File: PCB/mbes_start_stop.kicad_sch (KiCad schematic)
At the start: 17 parts

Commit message: fixes
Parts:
- RA41: renamed from RA?; value 10K -> 100K
- gave numbers to parts that had none: 16
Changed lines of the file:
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@@
   (symbol (lib_id "Connector_Generic:Conn_01x03") (at 159.2072 78.2828 0) (mirror x) (unit 1)
     (in_bom yes) (on_board yes) (fields_autoplaced)
-    (property "Reference" "koso-?" (id 0) (at 159.2072 71.882 0))
+    (property "Reference" "koso-1" (id 0) (at 159.2072 71.882 0))
     (property "Value" "Conn_01x03" (id 1) (at 162.4076 77.0129 0)
       (effects (font (size 1.27 1.27)) (justify left) hide)
@@
   (symbol (lib_id "Device:R") (at 138.2776 97.4852 90) (unit 1)
     (in_bom yes) (on_board yes)
-    (property "Reference" "RA?" (id 0) (at 138.2776 103.8352 90)
+    (property "Reference" "RA43" (id 0) (at 138.2776 103.8352 90)
       (effects (font (size 1.27 1.27)) hide)
     )
@@
   (symbol (lib_id "Transistor_BJT:BC337") (at 81.1784 145.5928 270) (unit 1)
     (in_bom yes) (on_board yes)
-    (property "Reference" "Q?" (id 0) (at 82.4485 150.9268 0)
+    (property "Reference" "Q11" (id 0) (at 82.4485 150.9268 0)
       (effects (font (size 1.27 1.27)) (justify left) hide)
     )
@@
   (symbol (lib_id "Device:R") (at 146.1008 130.4544 90) (unit 1)
     (in_bom yes) (on_board yes)
-    (property "Reference" "RA?" (id 0) (at 146.1008 136.8044 90)
+    (property "Reference" "RA44" (id 0) (at 146.1008 136.8044 90)
       (effects (font (size 1.27 1.27)) hide)
     )
@@
   (symbol (lib_id "power:GND") (at 122.5296 154.9908 0) (unit 1)
     (in_bom yes) (on_board yes) (fields_autoplaced)
-    (property "Reference" "#PWR?" (id 0) (at 122.5296 161.3408 0)
+    (property "Reference" "#PWR0108" (id 0) (at 122.5296 161.3408 0)
       (effects (font (size 1.27 1.27)) hide)
     )
@@
   (symbol (lib_id "Device:R") (at 95.9104 59.8932 180) (unit 1)
     (in_bom yes) (on_board yes)
-    (property "Reference" "RA?" (id 0) (at 102.2604 59.8932 90)
+    (property "Reference" "RA30" (id 0) (at 102.2604 59.8932 90)
       (effects (font (size 1.27 1.27)) hide)
     )
@@
   (symbol (lib_id "Device:R") (at 90.932 116.8908 180) (unit 1)
     (in_bom yes) (on_board yes)
-    (property "Reference" "RA?" (id 0) (at 97.282 116.8908 90)
+    (property "Reference" "RA29" (id 0) (at 97.282 116.8908 90)
       (effects (font (size 1.27 1.27)) hide)
     )
@@
   (symbol (lib_id "Transistor_BJT:BC327") (at 110.5408 76.4032 0) (mirror x) (unit 1)
     (in_bom yes) (on_board yes)
-    (property "Reference" "Q?" (id 0) (at 107.7468 74.1172 90)
+    (property "Reference" "Q18" (id 0) (at 107.7468 74.1172 90)
       (effects (font (size 1.27 1.27)) hide)
     )
@@
   (symbol (lib_id "Device:R") (at 90.932 107.1372 180) (unit 1)
     (in_bom yes) (on_board yes)
-    (property "Reference" "RA?" (id 0) (at 97.282 107.1372 90)
+    (property "Reference" "RA23" (id 0) (at 97.282 107.1372 90)
       (effects (font (size 1.27 1.27)) hide)
     )
@@
   (symbol (lib_id "power:GND") (at 153.2128 82.8548 0) (unit 1)
     (in_bom yes) (on_board yes) (fields_autoplaced)
-    (property "Reference" "#PWR?" (id 0) (at 153.2128 89.2048 0)
+    (property "Reference" "#PWR0106" (id 0) (at 153.2128 89.2048 0)
       (effects (font (size 1.27 1.27)) hide)
     )
@@
   (symbol (lib_id "Relay:RT42xxxx") (at 104.902 137.9728 90) (unit 1)
     (in_bom yes) (on_board yes)
-    (property "Reference" "K?" (id 0) (at 104.902 117.9068 90)
+    (property "Reference" "K1" (id 0) (at 104.902 117.9068 90)
       (effects (font (size 1.27 1.27)) hide)
     )
@@
   (symbol (lib_id "Device:R") (at 90.8304 83.82 180) (unit 1)
     (in_bom yes) (on_board yes)
-    (property "Reference" "RA?" (id 0) (at 97.1804 83.82 90)
+    (property "Reference" "RA8" (id 0) (at 97.1804 83.82 90)
       (effects (font (size 1.27 1.27)) hide)
     )
@@
   (symbol (lib_id "Device:R") (at 101.6508 76.4032 270) (unit 1)
     (in_bom yes) (on_board yes)
-    (property "Reference" "RA?" (id 0) (at 101.6508 70.0532 90)
+    (property "Reference" "RA33" (id 0) (at 101.6508 70.0532 90)
       (effects (font (size 1.27 1.27)) hide)
     )
@@
   (symbol (lib_id "Transistor_BJT:BC327") (at 98.9076 110.8964 0) (unit 1)
     (in_bom yes) (on_board yes)
-    (property "Reference" "Q?" (id 0) (at 96.1136 113.1824 90)
+    (property "Reference" "Q16" (id 0) (at 96.1136 113.1824 90)
       (effects (font (size 1.27 1.27)) hide)
     )
@@
   (symbol (lib_id "power:+12V") (at 120.142 54.4068 0) (unit 1)
     (in_bom yes) (on_board yes) (fields_autoplaced)
-    (property "Reference" "#PWR?" (id 0) (at 120.142 58.2168 0)
+    (property "Reference" "#PWR0102" (id 0) (at 120.142 58.2168 0)
       (effects (font (size 1.27 1.27)) hide)
     )
@@
   (symbol (lib_id "Device:R") (at 126.1872 113.538 0) (unit 1)
     (in_bom yes) (on_board yes)
-    (property "Reference" "RA?" (id 0) (at 119.8372 113.538 90)
-      (effects (font (size 1.27 1.27)) hide)
-    )
-    (property "Value" "10K" (id 1) (at 126.1872 113.538 90))
+    (property "Reference" "RA41" (id 0) (at 119.8372 113.538 90)
+      (effects (font (size 1.27 1.27)) hide)
+    )
+    (property "Value" "100K" (id 1) (at 126.1872 113.538 90))
     (property "Footprint" "Resistor_THT:R_Axial_DIN0207_L6.3mm_D2.5mm_P7.62mm_Horizontal" (id 2) (at 124.4092 113.538 90)
       (effects (font (size 1.27 1.27)) hide)
@@
   (symbol (lib_id "Device:R") (at 101.6508 65.1256 270) (unit 1)
     (in_bom yes) (on_board yes)
-    (property "Reference" "RA?" (id 0) (at 101.6508 58.7756 90)
+    (property "Reference" "RA31" (id 0) (at 101.6508 58.7756 90)
       (effects (font (size 1.27 1.27)) hide)
     )
@@
   (symbol (lib_id "Transistor_BJT:BC337") (at 90.8304 72.7456 270) (mirror x) (unit 1)
     (in_bom yes) (on_board yes)
-    (property "Reference" "Q?" (id 0) (at 92.1005 67.4116 0)
+    (property "Reference" "Q13" (id 0) (at 92.1005 67.4116 0)
       (effects (font (size 1.27 1.27)) (justify left) hide)
     )
@@
   (symbol (lib_id "Transistor_BJT:BC327") (at 110.5408 65.1256 0) (unit 1)
     (in_bom yes) (on_board yes)
-    (property "Reference" "Q?" (id 0) (at 107.7468 67.4116 90)
+    (property "Reference" "Q17" (id 0) (at 107.7468 67.4116 90)
       (effects (font (size 1.27 1.27)) hide)
     )
@@
   (symbol (lib_id "Transistor_BJT:BC337") (at 88.392 128.8288 0) (unit 1)
     (in_bom yes) (on_board yes)
-    (property "Reference" "Q?" (id 0) (at 84.963 125.6538 0)
-      (effects (font (size 1.27 1.27)) (justify left) hide)
-    )
+    (property "Reference" "Q12" (id 0) (at 84.963 125.6538 0)
+      (effects (font (size 1.27 1.27)) (justify left) hide)
+    )

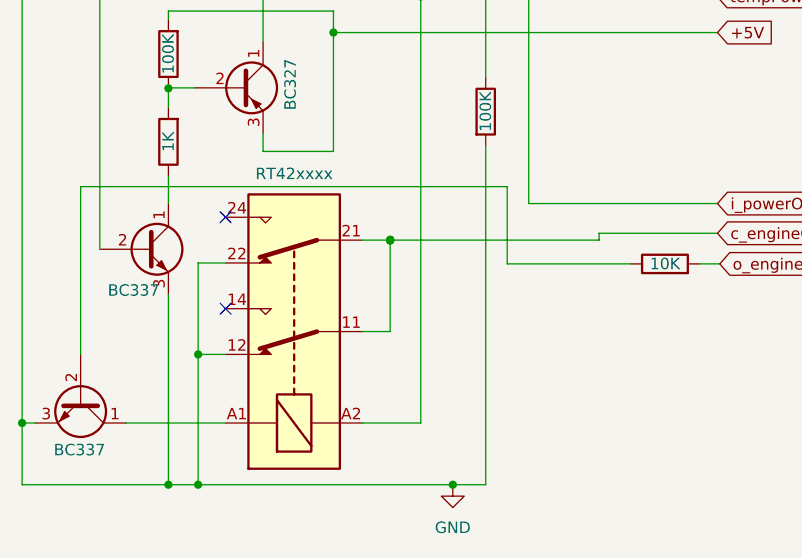
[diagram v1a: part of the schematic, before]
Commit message: Wrong relay's footprint fixed
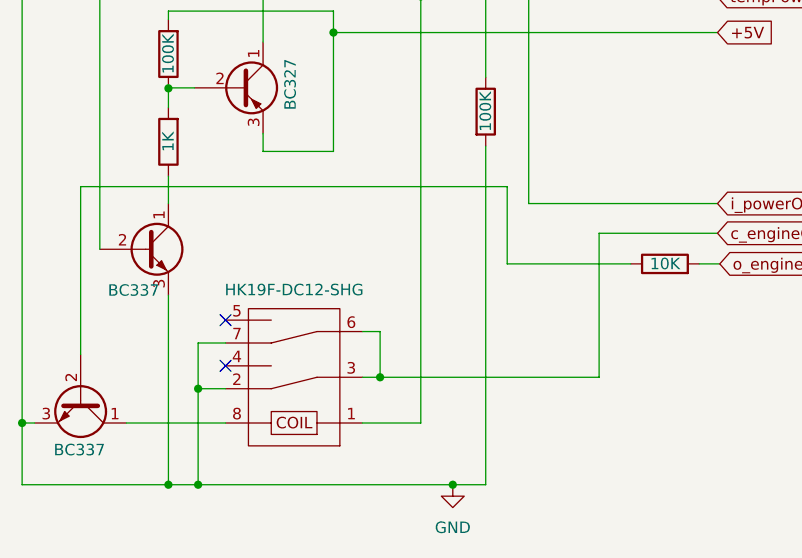
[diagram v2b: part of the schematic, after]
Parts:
- removed K1: RT42xxxx, Relay_THT:Relay_DPDT_Schrack-RT2-FormC_RM5mm, symbol Relay:RT42xxxx
- added U4: HK19F-DC12-SHG, HK19F:HK19F-DC12-SHG, symbol HK19F:HK19F-DC12-SHG
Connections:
- net GND: now also U4.2, U4.7
- net c_engineOFF: now also U4.3, U4.6
- net tempPower: now also U4.1
- net at Q11.1 (C): now also U4.8
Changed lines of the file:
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@@
   (junction (at 95.9104 65.1256) (diameter 0) (color 0 0 0 0)
   )
-  (junction (at 115.57 127.8128) (diameter 0) (color 0 0 0 0)
-  )
-  (junction (at 115.57 127.8636) (diameter 0) (color 0 0 0 0)
-  )
   (junction (at 90.932 110.9472) (diameter 0) (color 0 0 0 0)
   )
-  (junction (at 115.57 127.762) (diameter 0) (color 0 0 0 0)
+  (junction (at 94.234 144.3228) (diameter 0) (color 0 0 0 0)
+  )
+  (junction (at 114.4524 143.0528) (diameter 0) (color 0 0 0 0)
   )
   (junction (at 120.142 70.7136) (diameter 0) (color 0 0 0 0)
   )
-  (junction (at 94.234 140.5128) (diameter 0) (color 0 0 0 0)
-  )
   (junction (at 74.676 148.1328) (diameter 0) (color 0 0 0 0)
   )
@@
   (junction (at 90.8304 97.4852) (diameter 0) (color 0 0 0 0)
   )
-  (no_connect (at 97.282 125.2728))
-  (no_connect (at 97.282 135.4328))
+  (no_connect (at 97.282 141.7828))
+  (no_connect (at 97.282 136.7028))
   (wire (pts (xy 95.9104 76.4032) (xy 97.8408 76.4032))
     (stroke (width 0) (type default) (color 0 0 0 0))
@@
     (stroke (width 0) (type default) (color 0 0 0 0))
   )
-  (wire (pts (xy 115.57 127.8128) (xy 115.57 127.8636))
+  (wire (pts (xy 94.234 144.3228) (xy 97.282 144.3228))
     (stroke (width 0) (type default) (color 0 0 0 0))
   )
@@
     (stroke (width 0) (type default) (color 0 0 0 0))
   )
+  (wire (pts (xy 94.234 144.3228) (xy 94.234 154.9908))
+    (stroke (width 0) (type default) (color 0 0 0 0))
+  )
   (wire (pts (xy 90.932 120.7008) (xy 90.932 123.7488))
     (stroke (width 0) (type default) (color 0 0 0 0))
@@
     (stroke (width 0) (type default) (color 0 0 0 0))
   )
+  (wire (pts (xy 112.522 137.9728) (xy 114.4524 137.9728))
+    (stroke (width 0) (type default) (color 0 0 0 0))
+  )
   (wire (pts (xy 130.9624 97.4852) (xy 134.4676 97.4852))
     (stroke (width 0) (type default) (color 0 0 0 0))
@@
     (stroke (width 0) (type default) (color 0 0 0 0))
   )
+  (wire (pts (xy 94.234 139.2428) (xy 94.234 144.3228))
+    (stroke (width 0) (type default) (color 0 0 0 0))
+  )
   (wire (pts (xy 95.9104 65.1256) (xy 95.9104 70.2056))
     (stroke (width 0) (type default) (color 0 0 0 0))
@@
     (stroke (width 0) (type default) (color 0 0 0 0))
   )
-  (wire (pts (xy 112.522 137.9728) (xy 115.57 137.9728))
-    (stroke (width 0) (type default) (color 0 0 0 0))
-  )
   (wire (pts (xy 101.4476 100.7364) (xy 101.4476 105.8164))
     (stroke (width 0) (type default) (color 0 0 0 0))
   )
+  (wire (pts (xy 94.234 139.2428) (xy 97.282 139.2428))
+    (stroke (width 0) (type default) (color 0 0 0 0))
+  )
   (wire (pts (xy 113.0808 70.2056) (xy 113.0808 70.7136))
     (stroke (width 0) (type default) (color 0 0 0 0))
@@
     (stroke (width 0) (type default) (color 0 0 0 0))
   )
-  (wire (pts (xy 115.57 127.8636) (xy 115.57 137.9728))
-    (stroke (width 0) (type default) (color 0 0 0 0))
-  )
-  (wire (pts (xy 94.234 130.3528) (xy 94.234 140.5128))
+  (wire (pts (xy 114.4524 137.9728) (xy 114.4524 143.0528))
     (stroke (width 0) (type default) (color 0 0 0 0))
   )
@@
     (stroke (width 0) (type default) (color 0 0 0 0))
   )
-  (wire (pts (xy 112.522 127.8128) (xy 115.57 127.8128))
-    (stroke (width 0) (type default) (color 0 0 0 0))
-  )
   (wire (pts (xy 86.2584 148.1328) (xy 97.282 148.1328))
     (stroke (width 0) (type default) (color 0 0 0 0))
@@
     (stroke (width 0) (type default) (color 0 0 0 0))
   )
+  (wire (pts (xy 114.4524 143.0528) (xy 112.522 143.0528))
+    (stroke (width 0) (type default) (color 0 0 0 0))
+  )
   (wire (pts (xy 90.932 154.9908) (xy 94.234 154.9908))
     (stroke (width 0) (type default) (color 0 0 0 0))
@@
     (stroke (width 0) (type default) (color 0 0 0 0))
   )
-  (wire (pts (xy 115.57 127.762) (xy 115.57 127.8128))
-    (stroke (width 0) (type default) (color 0 0 0 0))
-  )
   (wire (pts (xy 93.8276 110.8964) (xy 90.932 110.8964))
     (stroke (width 0) (type default) (color 0 0 0 0))
@@
     (stroke (width 0) (type default) (color 0 0 0 0))
   )
-  (wire (pts (xy 94.234 140.5128) (xy 94.234 154.9908))
-    (stroke (width 0) (type default) (color 0 0 0 0))
-  )
   (wire (pts (xy 126.1872 97.4852) (xy 130.9624 97.4852))
     (stroke (width 0) (type default) (color 0 0 0 0))
@@
     (stroke (width 0) (type default) (color 0 0 0 0))
   )
-  (wire (pts (xy 138.7856 127.8128) (xy 115.57 127.8128))
-    (stroke (width 0) (type default) (color 0 0 0 0))
-  )
   (wire (pts (xy 151.9428 127.0508) (xy 138.7856 127.0508))
     (stroke (width 0) (type default) (color 0 0 0 0))
@@
     (stroke (width 0) (type default) (color 0 0 0 0))
   )
-  (wire (pts (xy 138.7856 127.0508) (xy 138.7856 127.8128))
+  (wire (pts (xy 138.7856 127.0508) (xy 138.7856 143.0528))
     (stroke (width 0) (type default) (color 0 0 0 0))
   )
@@
     (stroke (width 0) (type default) (color 0 0 0 0))
   )
-  (wire (pts (xy 97.282 130.3528) (xy 94.234 130.3528))
-    (stroke (width 0) (type default) (color 0 0 0 0))
-  )
   (wire (pts (xy 116.8908 78.2828) (xy 116.8908 83.566))
     (stroke (width 0) (type default) (color 0 0 0 0))
@@
     (stroke (width 0) (type default) (color 0 0 0 0))
   )
-  (wire (pts (xy 97.282 140.5128) (xy 94.234 140.5128))
-    (stroke (width 0) (type default) (color 0 0 0 0))
-  )
   (wire (pts (xy 109.2708 102.362) (xy 109.2708 104.7496))
+    (stroke (width 0) (type default) (color 0 0 0 0))
+  )
+  (wire (pts (xy 138.7856 143.0528) (xy 114.4524 143.0528))
     (stroke (width 0) (type default) (color 0 0 0 0))
   )
@@
     (pin "1")
   )
+  (symbol (lib_id "HK19F:HK19F-DC12-SHG") (at 106.172 155.7528 180) (unit 1)
+    (in_bom yes) (on_board yes) (fields_autoplaced)
+    (property "Reference" "U4" (id 0) (at 104.902 155.2956 0)
+      (effects (font (size 1.27 1.27)) hide)
+    )
+    (property "Value" "HK19F-DC12-SHG" (id 1) (at 104.902 133.35 0))
+    (property "Footprint" "HK19F:HK19F-DC12-SHG" (id 2) (at 106.172 155.7528 0)
+      (effects (font (size 1.27 1.27)) hide)
+    )
+    (property "Datasheet" "https://datasheetspdf.com/pdf-file/1015122/EVER-WAYINDUSTRY/HK19F-DC12V/1" (id 3) (at 106.172 155.7528 0)
+      (effects (font (size 1.27 1.27)) hide)
+    )
+    (pin "1")
+    (pin "2")
+    (pin "3")
+    (pin "4")
+    (pin "5")
+    (pin "6")
+    (pin "7")
+    (pin "8")
+  )
   (symbol (lib_id "Device:R") (at 95.9104 59.8932 180) (unit 1)
     (in_bom yes) (on_board yes)
@@
     (pin "1")
   )
-  (symbol (lib_id "Relay:RT42xxxx") (at 104.902 137.9728 90) (unit 1)
-    (in_bom yes) (on_board yes)
-    (property "Reference" "K1" (id 0) (at 104.902 117.9068 90)
-      (effects (font (size 1.27 1.27)) hide)
-    )
-    (property "Value" "RT42xxxx" (id 1) (at 104.902 120.4468 90))
-    (property "Footprint" "Relay_THT:Relay_DPDT_Schrack-RT2-FormC_RM5mm" (id 2) (at 104.902 137.9728 0)
-      (effects (font (size 1.27 1.27)) hide)
-    )
-    (property "Datasheet" "http://www.te.com/commerce/DocumentDelivery/DDEController?Action=showdoc&DocId=Data+Sheet%7FRT2%7F1014%7Fpdf%7FEnglish%7FENG_DS_RT2_1014.pdf%7F6-1393243-3" (id 3) (at 104.902 137.9728 0)
-      (effects (font (size 1.27 1.27)) hide)
-    )
-    (pin "11")
-    (pin "12")
-    (pin "14")
-    (pin "21")
-    (pin "22")
-    (pin "24")
-    (pin "A1")
-    (pin "A2")
-  )
   (symbol (lib_id "Device:R") (at 90.8304 83.82 180) (unit 1)

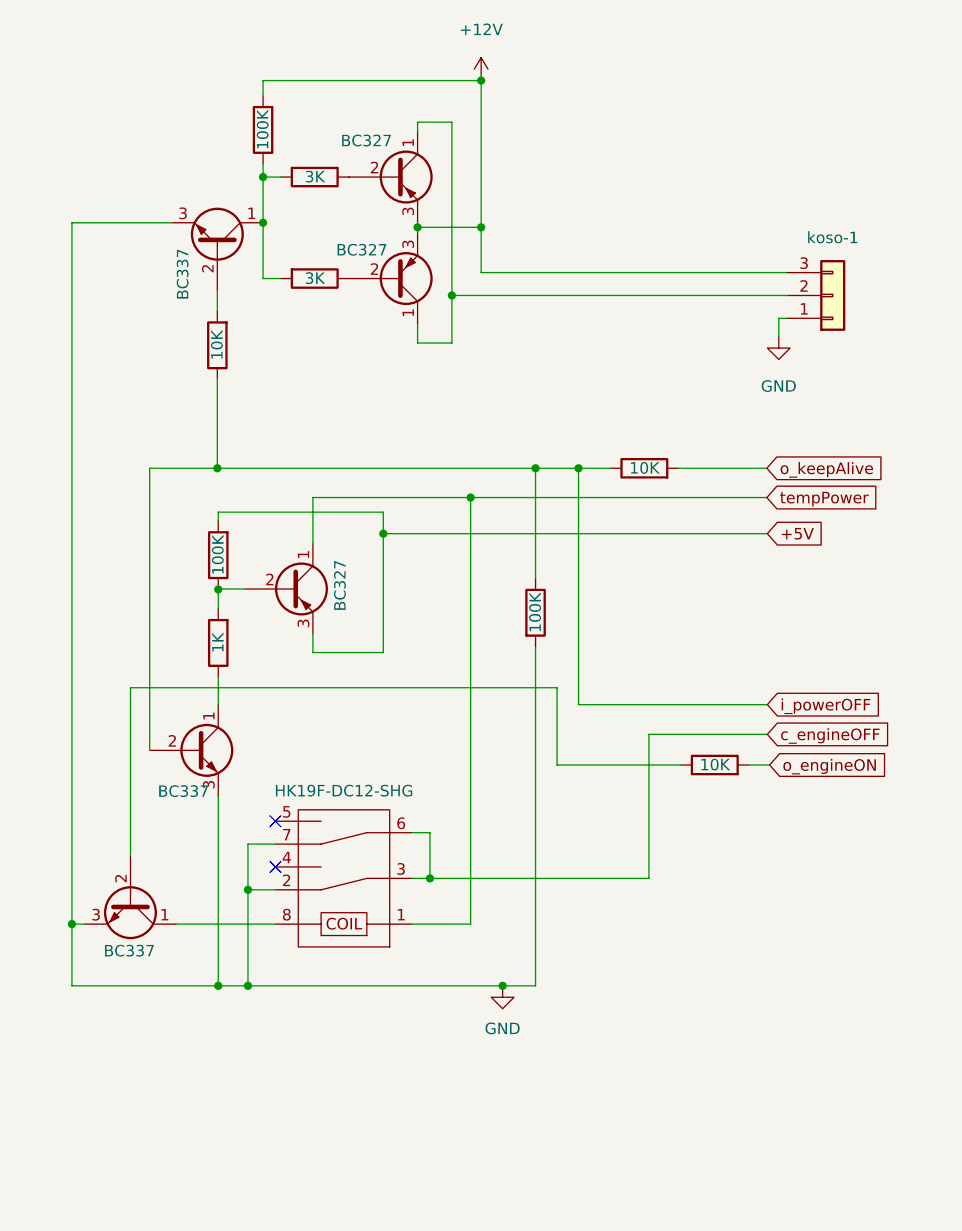
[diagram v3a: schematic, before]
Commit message: Fix and changes for self-power-suppling system
Because the PCB-B should be responsible just for power switching management and PCB-A for the control logic, the
self-power-suppling system has been moved from pcb-b to pcb-a. It should be easier to debug too
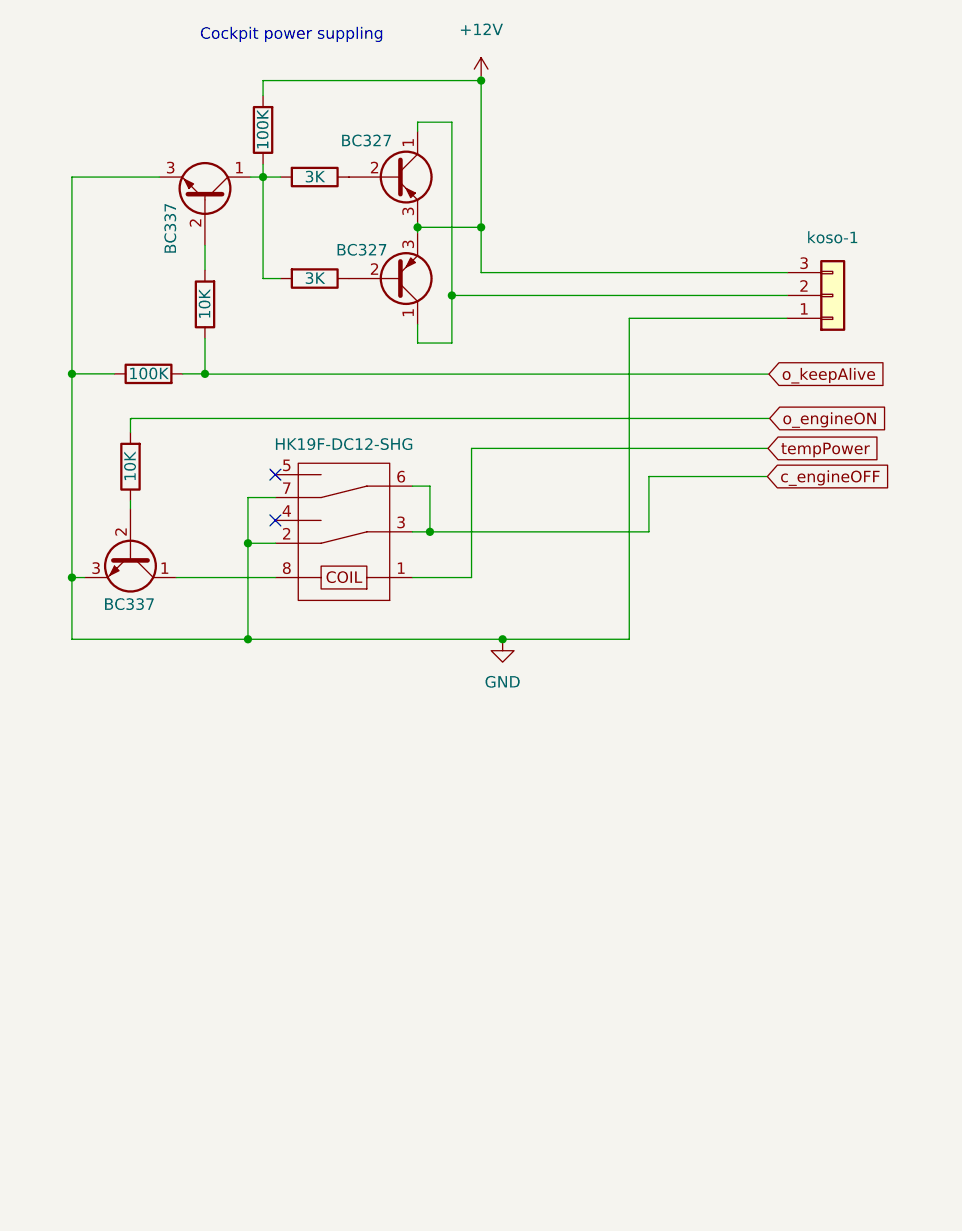
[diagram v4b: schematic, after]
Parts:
- removed Q12: BC337, Package_TO_SOT_THT:TO-92L_Inline_Wide, symbol Transistor_BJT:BC337
- removed Q16: BC327, Package_TO_SOT_THT:TO-92L_Inline_Wide, symbol Transistor_BJT:BC327
- removed RA23: 100K, Resistor_THT:R_Axial_DIN0207_L6.3mm_D2.5mm_P7.62mm_Horizontal, symbol Device:R
- removed RA29: 1K, Resistor_THT:R_Axial_DIN0207_L6.3mm_D2.5mm_P7.62mm_Horizontal, symbol Device:R
- removed RA43: 10K, Resistor_THT:R_Axial_DIN0207_L6.3mm_D2.5mm_P7.62mm_Horizontal, symbol Device:R
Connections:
- net GND: now also RA41.1; no longer RA41.2
- net o_keepAlive: now also RA41.2, RA8.1
- removed net i_powerOFF: RA41.1, RA8.1
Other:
- note added: "Cockpit power suppling"

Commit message: Merged files
These files have been merged by remotes/origin/ATmega16__dualPCB__bluetoothCockpit branch
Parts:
- removed Q11, Q13: BC337, Package_TO_SOT_THT:TO-92L_Inline_Wide, symbol Transistor_BJT:BC337
- added Q10, Q12: BC817, Package_TO_SOT_SMD:SOT-23, symbol Transistor_BJT:BC817
- added RA43: 10K, Resistor_SMD:R_1206_3216Metric, symbol Device:R
- RA30, RA31, RA33, RA41, RA44, RA8: footprint Resistor_THT:R_Axial_DIN0207_L6.3mm_D2.5mm_P7.62mm_Horizontal -> Resistor_SMD:R_1206_3216Metric
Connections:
- net GND: now also RA41.2, Q10.2 (E), Q12.2 (E); no longer RA41.1
- net o_keepAlive: now also RA43.2; no longer RA41.2, RA8.1
- net at U4.8: now also Q12.3 (C)
- net at RA44.1: now also Q12.1 (B)
- net at RA30.1, RA31.2, RA33.2: now also Q10.3 (C)
- net at RA8.2: now also Q10.1 (B)
- new net i_powerOFF: RA41.1, RA43.1, RA8.1
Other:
- note added: "CDI"
- note removed: "Cockpit power suppling"
- moved on the sheet: koso-1
